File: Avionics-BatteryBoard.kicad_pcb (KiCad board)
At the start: 4 copper layers, 90.2 x 95.9 mm, 122 parts, among them J1 21700 Holder, J2 Fuel Gauge Programming Header, J3 205338-0002, J4 205338-0004, J7 QTH-030-01-L-D-A, J8 522711069, Q1 SIRA99DP-T1-GE3, Q10 IRLML2803, Q11 SIRA99DP-T1-GE3, Q12 IRLML2803, Q2 SIRA99DP-T1-GE3, Q3 SIRA99DP-T1-GE3, Q4 SIRA99DP-T1-GE3, Q5 MBT2222ADW1T1, Q6 MBT2222ADW1T1, Q7 NX3008NBKS, Q8 NX3008NBKS, Q9 SIRA99DP-T1-GE3, U1 S-8209AAA-T8T1U, U2 S-8209AAA-T8T1U, U3 MAX17205, U4 LTC4412xS6, U5 LTC4412xS6, U6 TLX9000, U7 TLX9000

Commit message: v4.0 done 500x
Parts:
- added MP1: M3 x 5mm, Argus-Misc:WA-SMSI_9774050360, F.Cu at (174.0, 81.6)
- added MP2: M3 x 5mm, Argus-Misc:WA-SMSI_9774050360, F.Cu at (174.0, 112.1)
- moved J3 56.4 mm to (177.8, 121.9)
- moved TH1 49.2 mm to (172.0, 122.3)
- moved TH3 49.2 mm to (150.4, 122.4)
- moved R27 44.2 mm to (147.0, 99.1), turned to -90 degrees
- moved R31 42.0 mm to (148.6, 99.1), turned to -90 degrees
- moved R18 41.0 mm to (145.6, 103.9), turned to 90 degrees
- moved R32 39.7 mm to (147.9, 101.6), turned to 0 degrees
- moved Q6 38.7 mm to (151.0, 99.2), turned to -90 degrees
- moved R17 37.9 mm to (159.8, 94.1), turned to 90 degrees
- moved R34 37.8 mm to (147.9, 103.2), turned to 0 degrees
- moved R37 36.7 mm to (152.9, 99.0), turned to 90 degrees
- moved C12 36.2 mm to (147.9, 104.7), turned to 180 degrees
- moved R28 35.4 mm to (150.8, 101.5), turned to 180 degrees
- moved Q8 34.3 mm to (154.9, 99.2), turned to 90 degrees
- moved C13 33.0 mm to (158.0, 98.5), turned to 0 degrees
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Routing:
- net /Interfaces/SDA_BUS: track 156.8 -> 82.7 mm, vias 3 -> 4
- net /Battery Monitor/SDA: track 78.9 -> 28.9 mm
- net /Interfaces/SCL_BUS: track 139.5 -> 97.8 mm
- net /Battery Monitor/SCL: track 63.6 -> 34.5 mm
- net /Battery Bus Protection/DISCHARGE_ACTIVE: track 58.9 -> 32.2 mm
- net /Battery Bus Protection/CHARGE_ACTIVE: track 45.9 -> 21.4 mm
- net Net-(U3-AIN2): track 34.9 -> 59.3 mm
- net /Interfaces/ALERT: track 124.8 -> 104.8 mm
- net Net-(U3-AIN1): track 81.0 -> 93.7 mm
- net Net-(R40-Pad1): track 10.7 -> 23.3 mm
- net /Battery Bus Detection/CHARGE_EN: track 34.7 -> 25.5 mm
- net +3V3: track 30.0 -> 21.5 mm, vias 12 -> 15
- net Net-(R44-Pad1): track 12.1 -> 20.4 mm
- net Net-(R53-Pad1): track 12.1 -> 20.3 mm
- net Net-(R54-Pad1): track 12.1 -> 20.2 mm
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- added copper zone on In2.Cu, net +3V3
- added copper zone on In1.Cu, net SYSTEM_VDD
- removed copper zone on In1.Cu, net +3V3
- removed copper zone on In2.Cu, net SYSTEM_VDD
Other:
- outline, holes or cut-outs redrawn

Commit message: ready to order v4.0
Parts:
- added kibuzzard-6A91DD42: G***, kibuzzard-6A91DD42, F.Cu at (128.4, 122.6)
- added kibuzzard-6A91DD5B: G***, kibuzzard-6A91DD5B, F.Cu at (145.7, 122.7)
- moved kibuzzard-6A825BB0 0.36 mm to (103.3, 109.7)
- moved kibuzzard-6A825BF2 0.36 mm to (103.4, 112.9)
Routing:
- net +3V3: track 21.5 -> 18.1 mm, vias 15 -> 4
- net /Interfaces/SDA_BUS: track 82.7 -> 83.5 mm
- net Net-(U3-AIN2): track 59.3 -> 59.9 mm
- net /Interfaces/SCL_BUS: track 97.8 -> 98.3 mm
- removed copper zone on In2.Cu, net +3V3

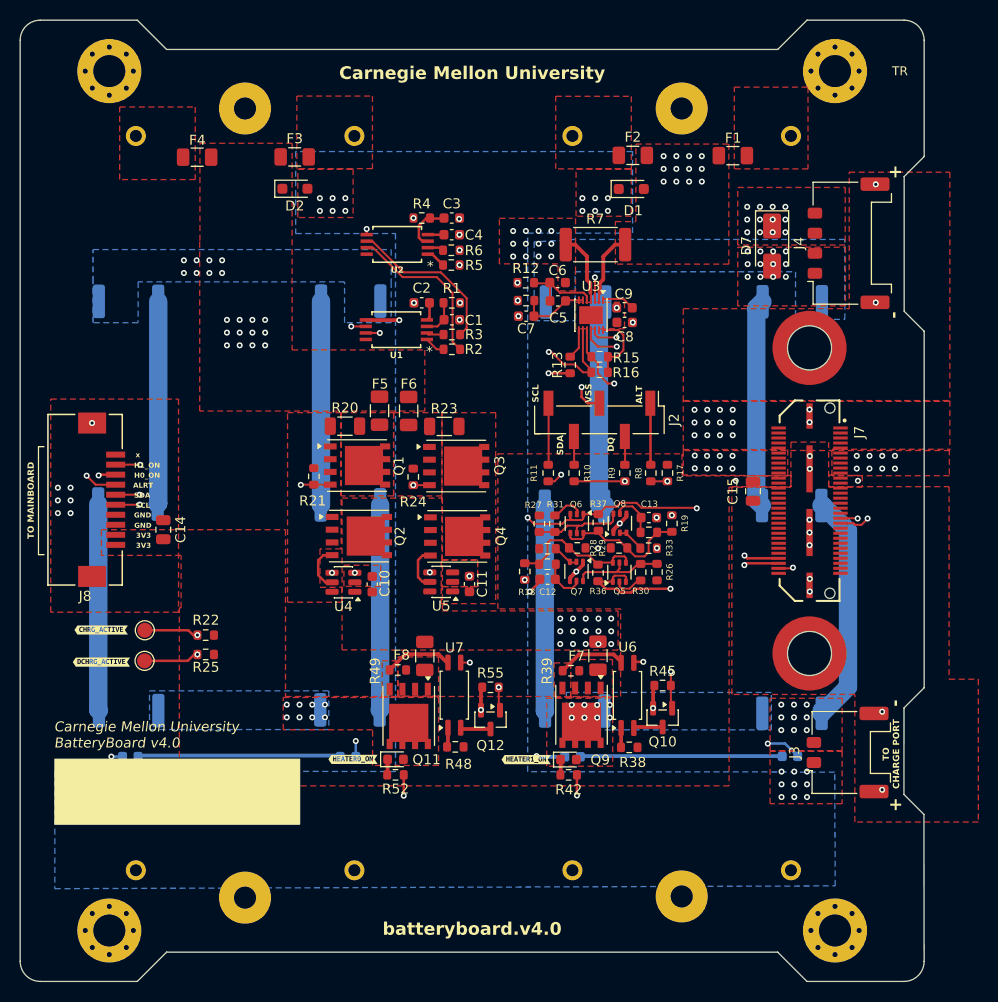
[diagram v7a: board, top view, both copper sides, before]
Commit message: fixed up silkscreen stuff
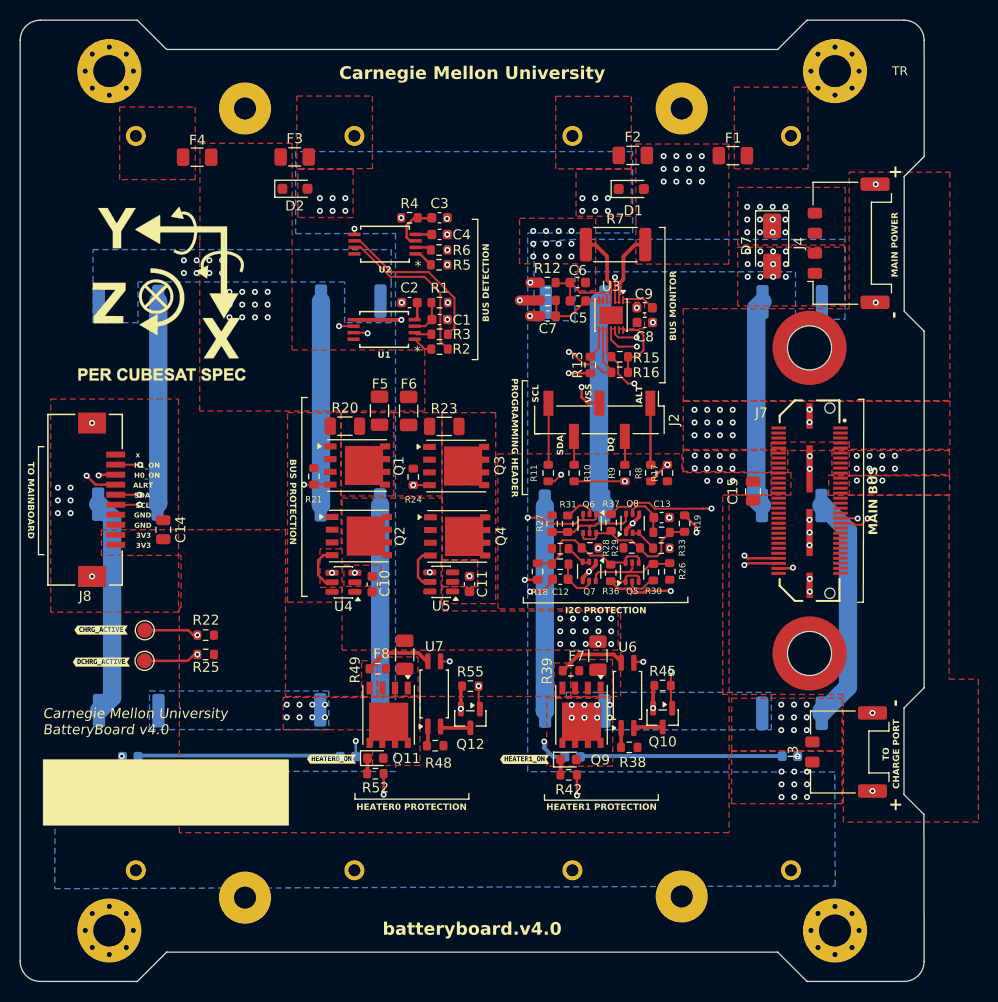
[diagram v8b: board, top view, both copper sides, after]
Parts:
- added REF**: Val**, mainboard:XYZ_cubesat-bot, B.Cu at (109.4, 76.2)
- moved C7 2.15 mm to (147.9, 78.4)
- moved R14 2.15 mm to (147.9, 76.8)
- moved R12 2.15 mm to (147.8, 75.1)
- moved kibuzzard-6A91DD42 2.13 mm to (126.3, 122.6)
- moved U7 2.01 mm to (136.6, 116.1)
- moved D6 2.01 mm to (130.7, 122.5)
- moved Q12 2.01 mm to (140.2, 118.5)
- moved R49 2.01 mm to (130.9, 113.6)
- moved R55 2.01 mm to (140.2, 115.3)
- moved F8 2.01 mm to (133.6, 112.2)
- moved Q11 2.01 mm to (132.0, 118.2)
- moved R48 2.01 mm to (136.6, 121.3)
- moved R52 2.01 mm to (130.7, 124.1)
- moved C5 2.01 mm to (150.9, 76.9)
- moved C6 2.01 mm to (150.9, 75.1)
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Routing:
- net Net-(U3-AIN2): track 59.9 -> 53.2 mm
- net /Battery Monitor/SDA: track 28.9 -> 35.5 mm
- net +3V3: track 18.1 -> 24.7 mm, vias 4 -> 8
- net /Battery Bus Detection/BATT_M: track 3.36 -> 6.81 mm
- net /Battery Bus Detection/BATT_N: track 20.2 -> 22.5 mm
- net /Interfaces/ALERT: track 104.8 -> 102.8 mm
- net /Interfaces/SCL_BUS: track 98.3 -> 96.9 mm
- net GND: track 11.2 -> 12.5 mm, vias 26 -> 27
- net /Battery Bus Detection/DISCHARGE_EN: track 23.8 -> 25.1 mm
- net Net-(R51-Pad1): track 20.6 -> 21.7 mm
- net Net-(U3-AIN1): track 93.7 -> 94.7 mm
- net /Battery Bus Detection/BATT_P: track 0.00 -> 0.95 mm
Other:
- board text added: "BUS DETECTION"
- board text added: "BUS MONITOR"
- board text added: "BUS PROTECTION"
- board text added: "HEATER0 PROTECTION"
- board text added: "HEATER1 PROTECTION"
- board text added: "I2C PROTECTION"
- board text added: "MAIN BUS"
- board text added: "MAIN POWER"
- board text added: "PROGRAMMING HEADER"
